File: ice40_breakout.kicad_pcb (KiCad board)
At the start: 4 copper layers, 80 x 100 mm, 240 parts, among them J1 Conn_01x10, J2 Conn_01x08, J3 Conn_01x06, J4 Conn_01x08, J5 USB_B_Micro, J6 7-17 V IN, Q1 DMP3099L-7, Q2 Q_NMOS_GSD, Q3 Q_NMOS_GSD, Q4 Q_NMOS_GSD, SW1 SW_Push, SW2 SW_Push, SW3 SW_Push, SW4 SW_Push, SW5 SW_Push, SW6 SW_Push, SW7 JS202011SCQN, SW8 JS202011SCQN, SW9 JS202011SCQN, U1 ICE40HX4K-TQ144, U10 MAX40200AUK, U11 SN74LVC2G07DCKR, U12 TPS562201, U13 SN74AXC4T245PWR, U14 MIC5365-3.3YC5, U15 MAX40200AUK, U16 SN74LVC2T45DCUR, U17 SN74LVC2T45DCUR, U18 SN74LVC2T45DCUR, U19 SN74LVC2T45DCUR, U2 IS61WV5128EDBLL-10TLI, U20 MAX11614, U21 MAX40200AUK, U22 MAX40200AUK, U3 93LCxxBT-I_OT, U4 FT2232H, U5 IS25LP080D, U6 TLV62568APDRLR, U7 TLV62568APDRLR, U8 TXS0108EPW, U9 TXS0108EPW, Y1 ECS-3225S33-120-FN-TR, Y2 ECS-3225S33-500-FN-TR

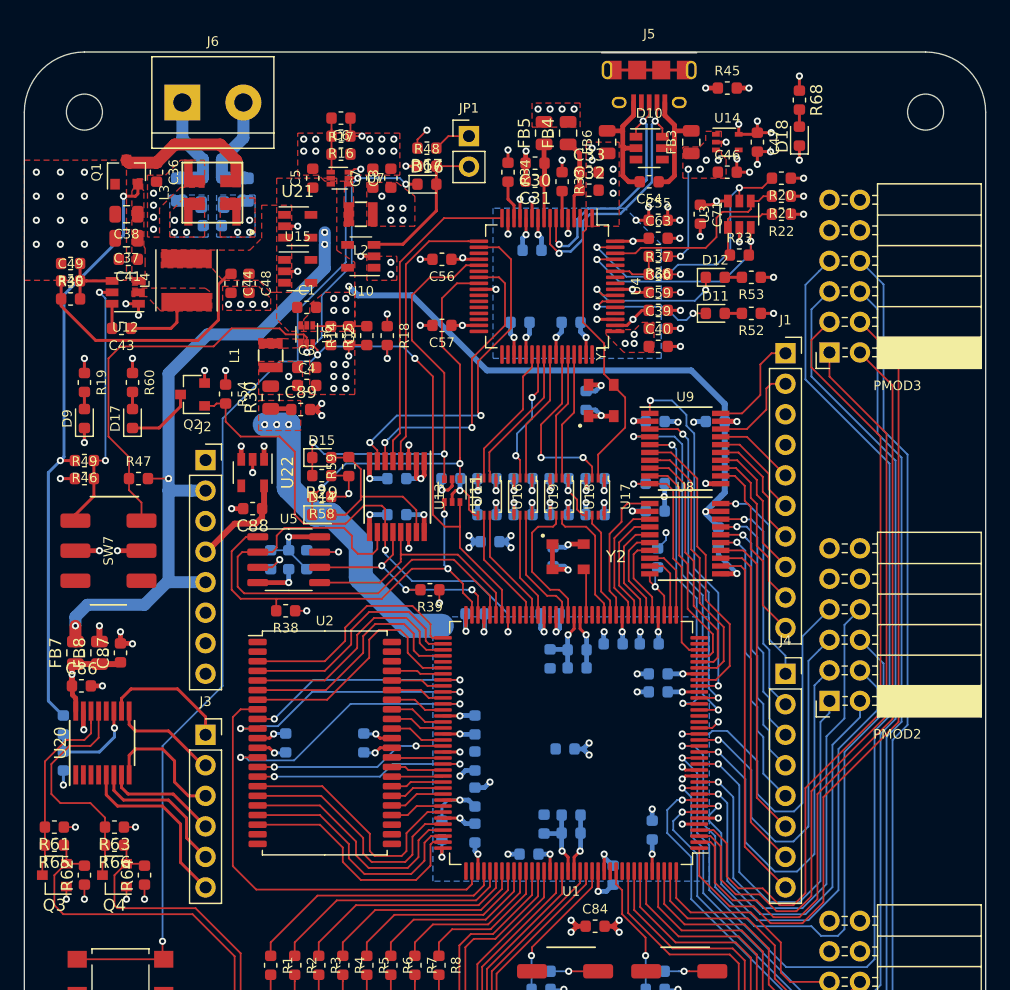
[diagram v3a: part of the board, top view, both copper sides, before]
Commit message: Added more BOM information, updated fpga symbol, added some more 3d models
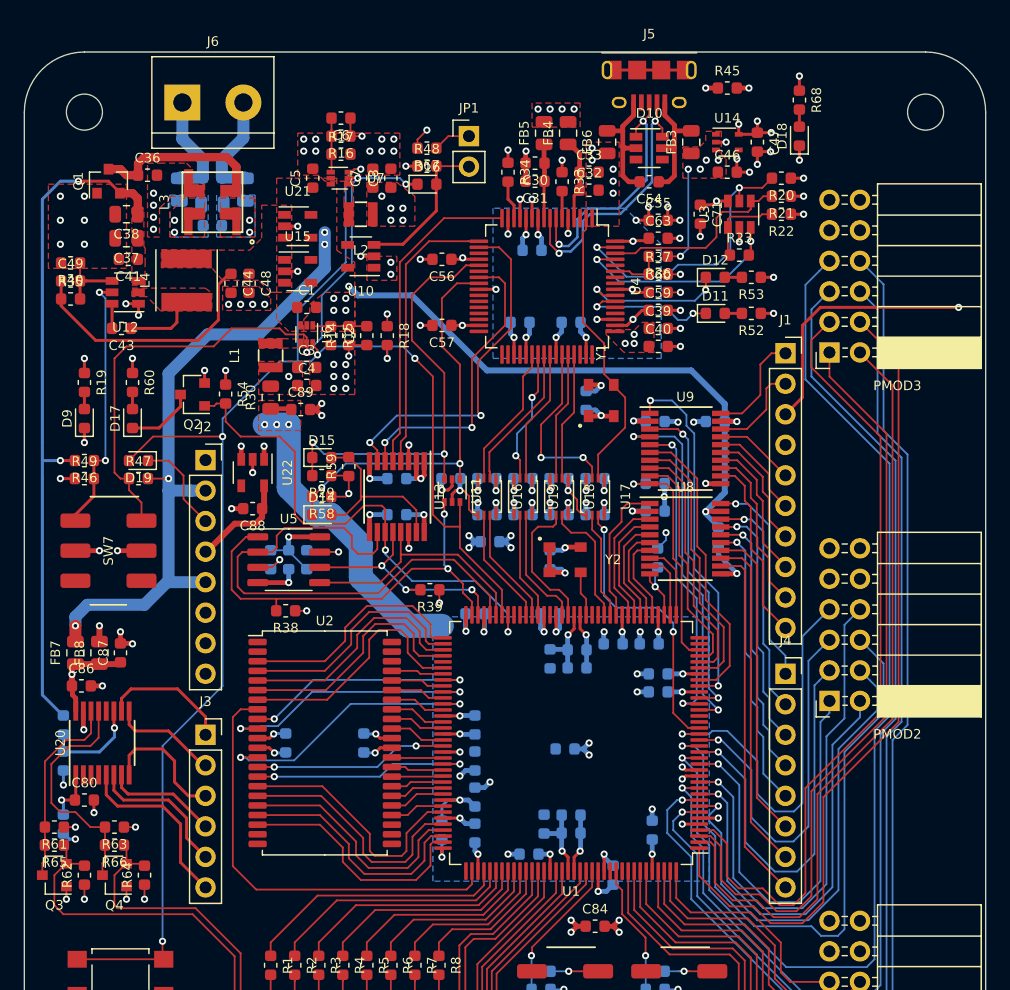
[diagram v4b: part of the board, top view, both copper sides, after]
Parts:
- added C80: 100nF, Capacitor_SMD:C_0603_1608Metric, F.Cu at (105.0, 102.2)
- added D19: CDBU5020, Diode_SMD:D_0603_1608Metric, F.Cu at (109.5, 74.0)
- added R70: 1k, Resistor_SMD:R_0603_1608Metric, B.Cu at (103.2, 104.2)
- moved Q1 1.68 mm to (107.0, 50.8)
- moved L3 0.80 mm to (115.7, 52.5)
- moved C36 0.79 mm to (110.2, 50.2), turned to 0 degrees
- moved C73 0.35 mm to (143.8, 82.2)
- moved Y2 0.35 mm to (145.0, 82.2)
- moved R40 0.05 mm to (103.8, 57.5)
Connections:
- J1 pad 3: (no net) -> /Header/INO_AREF
- J2 pad 3: (no net) -> /Header/INO_RESET
- U20 pad 1: (no net) -> Net-(C80-Pad1)
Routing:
- net /Header/INO_AREF: track 0.00 -> 188.7 mm, vias 0 -> 2
- net ICE_CLK_12M: track 1.79 -> 23.8 mm, vias 1 -> 2
- net CRESET_B: track 123.1 -> 131.7 mm, vias 5 -> 6
- net /Header/INO_RESET: track 0.00 -> 8.03 mm
- net V_IN_PROTECTED: track 49.6 -> 56.9 mm
- net Net-(C80-Pad1): track 0.00 -> 4.51 mm, vias 0 -> 1
- net /power/V_IN_CHOKE: track 11.5 -> 13.7 mm
- net GND: track 186.7 -> 187.7 mm, vias 170 -> 164
- net Net-(J5-Pad6): track 6.76 -> 7.39 mm
- net /power/V_IN_FILTERED: vias 3 -> 2
- net /power/GND_IN_FILTERED: vias 3 -> 2

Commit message: More BOM Information, more 3d Models
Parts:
- C10, C11, C12, C13, C14, C15, C16, C17, C18, C19, C20, C21, C22, C23, C24, C25, C26, C27, C28, C29, C30, C32, C39, C42, C43, C45, C51, C53, C56, C57, C58, C59, C60, C61, C62, C63, C64, C66, C67, C68, C69, C70, C71, C72, C73, C74, C75, C76, C77, C78, C79, C80, C81, C82, C85, C86, C9: value 100nF -> 100nF 6,3 V
- C2, C49, C6: value 10pF -> 10pF 6,3 V
- C35, C36, C41: value 100nF -> 100nF 25 V

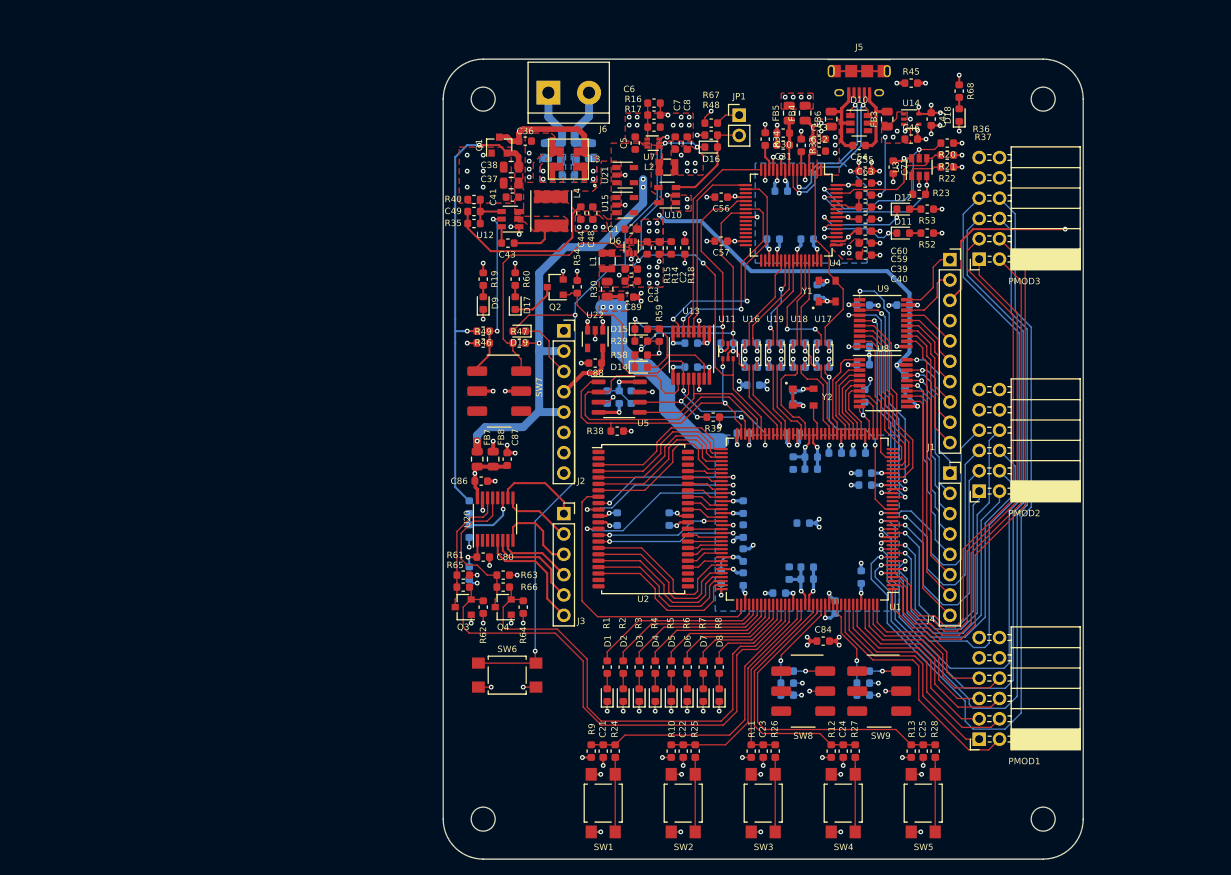
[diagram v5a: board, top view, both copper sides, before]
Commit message: Corrected a few footprints
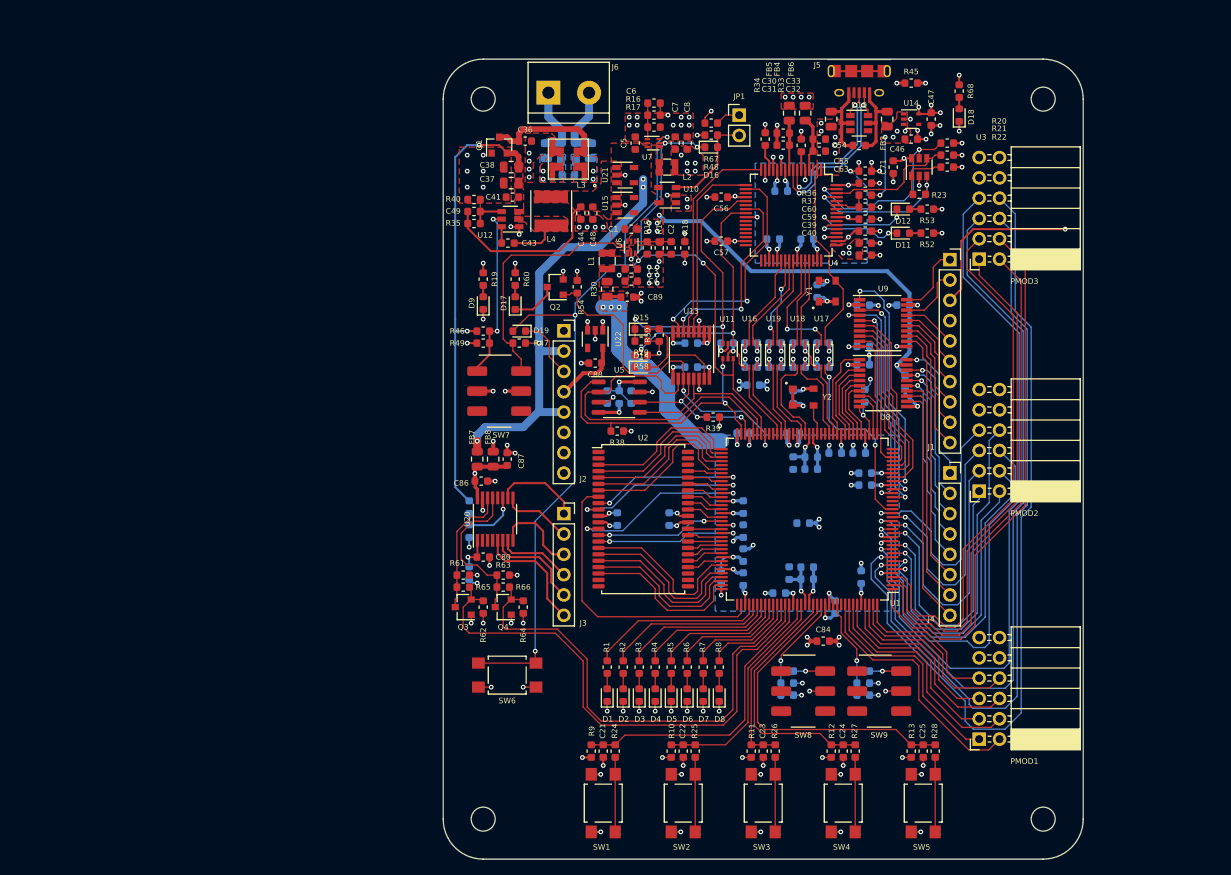
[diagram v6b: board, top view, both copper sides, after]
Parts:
- L3: footprint footprints:DLW5BTM_5.00x5.00mm_footprint -> footprints:L_Murata_DLW5BTM_5.00x5.00mm_footprint
- U6, U7: footprint Package_TO_SOT_SMD:SOT-563 -> footprints:Texas_DRL_SOT-563_1.6x1.6mm_0.5mm-pitch_footprint
- Y1, Y2: footprint footprints:ECS-3225S_3.2x2.5mm_footprint -> footprints:Y_ECS-3225S_3.2x2.5mm_footprint
- turned L3 to 180 degrees
- turned SW7 to 0 degrees
- turned SW8 to 0 degrees
- turned SW9 to 0 degrees
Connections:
- SW7 pad 1: /power/EN_LOW_VOLTAGE -> /power/EN_HIGH_VOLTAGE
- SW7 pad 4: /power/EN_HIGH_VOLTAGE -> /power/EN_LOW_VOLTAGE
- SW8 pad 1: Net-(R56-Pad2) -> (no net)
- SW8 pad 2: GND -> (no net)
- SW8 pad 4: (no net) -> Net-(R56-Pad2)
- SW8 pad 5: (no net) -> GND
- SW9 pad 1: Net-(R57-Pad2) -> (no net)
- SW9 pad 2: GND -> (no net)
- SW9 pad 4: (no net) -> Net-(R57-Pad2)
- SW9 pad 5: (no net) -> GND
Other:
- rule pad_to_mask_clearance: 0.051 -> 0.15
- rule via_min_size: 0.4 -> 0.6

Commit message: Finished Silkscreen and added layer markings as specified by manufacturer
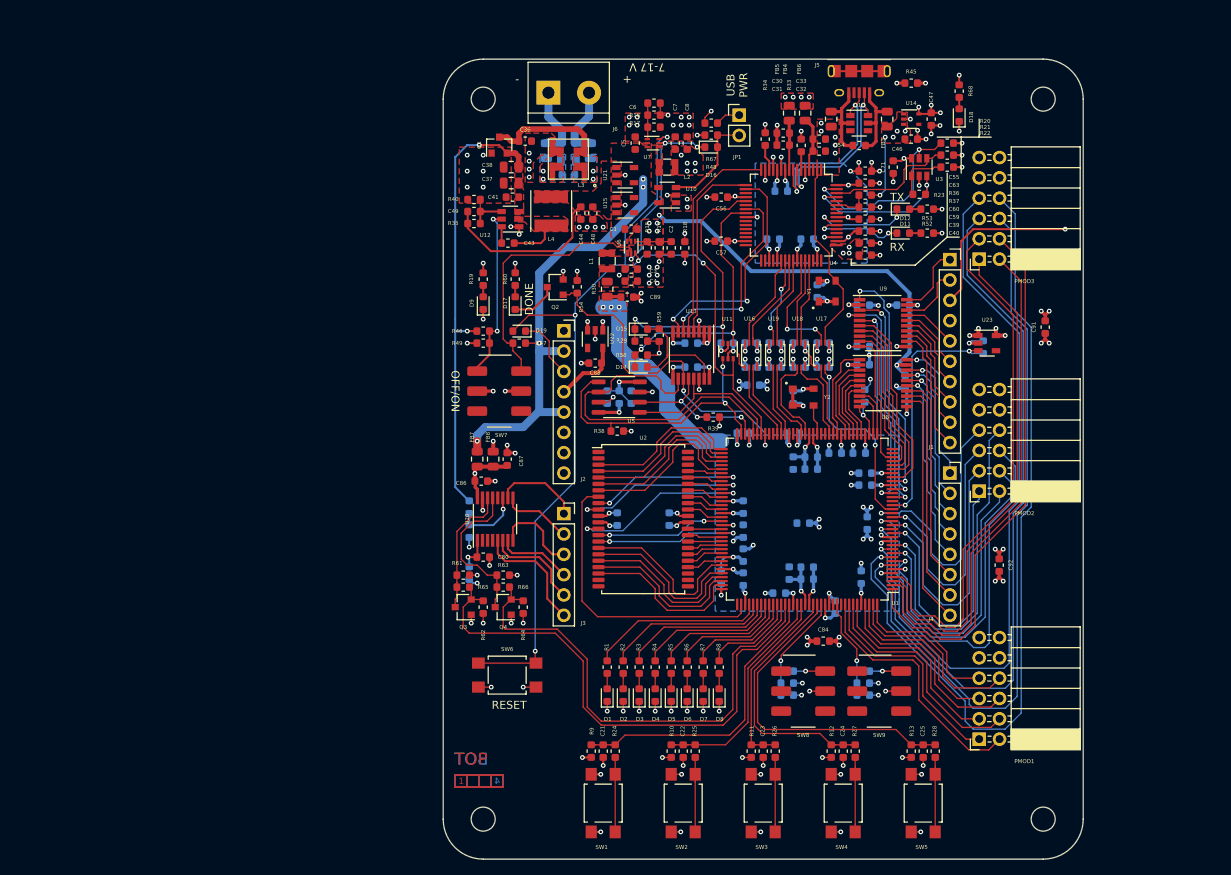
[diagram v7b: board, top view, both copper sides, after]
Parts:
- added C90: 10 uF 6,3 V, Capacitor_SMD:C_0603_1608Metric, B.Cu at (153.0, 98.0)
- added C91: 10 uF 6,3 V, Capacitor_SMD:C_0603_1608Metric, F.Cu at (175.2, 73.5)
- added C92: 10 uF 6,3 V, Capacitor_SMD:C_0603_1608Metric, F.Cu at (169.5, 103.2)
- added R71: 10k, Resistor_SMD:R_0603_1608Metric, B.Cu at (167.5, 76.0)
- added U23: MAX40200AUK, Package_TO_SOT_SMD:SOT-23-5, F.Cu at (168.0, 75.5)
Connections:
- D10 pad 1: /USB Programmer/D_N -> /USB Programmer/D_P
- D10 pad 6: /USB Programmer/D_P -> /USB Programmer/D_N
- J5 pad 2: /USB Programmer/D_P -> /USB Programmer/D_N
- J5 pad 3: /USB Programmer/D_N -> /USB Programmer/D_P
- PMOD1 pad 11: +3V3 -> /Header/PMOD_3V3
- PMOD1 pad 12: +3V3 -> /Header/PMOD_3V3
- PMOD2 pad 11: +3V3 -> /Header/PMOD_3V3
- PMOD2 pad 12: +3V3 -> /Header/PMOD_3V3
- PMOD3 pad 11: +3V3 -> /Header/PMOD_3V3
- PMOD3 pad 12: +3V3 -> /Header/PMOD_3V3
- U1 pad 22: (no net) -> /Header/PMOD_PWR_EN
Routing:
- net /Header/PMOD_PWR_EN: track 0.00 -> 31.0 mm, vias 0 -> 2
- net GND: track 187.7 -> 198.3 mm, vias 164 -> 172
- net /Header/PMOD_3V3: track 0.00 -> 6.30 mm, vias 0 -> 6
- net +3V3: track 95.5 -> 99.6 mm, vias 51 -> 55
- net /USB Programmer/D_N: track 21.1 -> 22.3 mm
- net /power/V_IN_CHOKE: track 13.7 -> 14.6 mm
- net /Header/INO_AREF: track 188.7 -> 187.9 mm
- net /USB Programmer/D_P: track 22.7 -> 23.2 mm
- added copper zone on In2.Cu, net /Header/PMOD_3V3
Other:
- board text added: "+"
- board text added: "-"
- board text added: "1"
- board text added: "2"
- board text added: "3"
- board text added: "4"
- board text added: "7-17 V"
- board text added: "BOT"
- board text added: "DONE"
- board text added: "OFF/ON"
- board text added: "RESET"
- board text added: "RX"
- board text added: "TOP"
- board text added: "TX"
- board text added: "USB PWR"

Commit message: Produktionsdaten
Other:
- rule solder_mask_min_width: 0.25 -> 0.1
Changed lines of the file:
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@@
     (32 B.Adhes user hide)
     (33 F.Adhes user hide)
-    (34 B.Paste user hide)
-    (35 F.Paste user hide)
+    (34 B.Paste user)
+    (35 F.Paste user)
     (36 B.SilkS user)
     (37 F.SilkS user)
@@
     (46 B.CrtYd user)
     (47 F.CrtYd user)
-    (48 B.Fab user)
-    (49 F.Fab user)
+    (48 B.Fab user hide)
+    (49 F.Fab user hide)
   )
   (setup
@@
     (pad_drill 0.762)
     (pad_to_mask_clearance 0.15)
-    (solder_mask_min_width 0.25)
+    (solder_mask_min_width 0.1)
+    (pad_to_paste_clearance_ratio -0.05)
     (aux_axis_origin 0 0)
     (grid_origin 100 140)
@@
     (pcbplotparams
       (layerselection 0x010fc_ffffffff)
-      (usegerberextensions false)
+      (usegerberextensions true)
       (usegerberattributes false)
       (usegerberadvancedattributes false)
@@
       (psa4output false)
       (plotreference true)
-      (plotvalue true)
+      (plotvalue false)
       (plotinvisibletext false)
       (padsonsilk false)
-      (subtractmaskfromsilk false)
+      (subtractmaskfromsilk true)
       (outputformat 1)
       (mirror false)
-      (drillshape 1)
+      (drillshape 0)
       (scaleselection 1)
-      (outputdirectory ""))
+      (outputdirectory "fab/"))
   )
   (net 0 "")
